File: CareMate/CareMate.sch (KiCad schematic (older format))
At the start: 19 parts, among them J1 Barrel_Jack_MountingPin, J2 Conn_01x16, J3 Conn_01x03, J4 Conn_01x03, J5 Conn_01x06, J6 Conn_01x03, J7 Conn_01x03, J8 Conn_01x02, J9 Conn_01x16, U1 L7805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

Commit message: began running traces
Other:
- note removed: "*Pull up resistor on SD Card Reader\n**Additional Microphone Connect to elechouse and ESP\n***Limit Switch\n****5V Regulator"
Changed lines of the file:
@@
 Wire Wire Line
 	10350 1700 10250 1700
-Text Notes 900  3500 0    50   ~ 0
-*Pull up resistor on SD Card Reader\n**Additional Microphone Connect to elechouse and ESP\n***Limit Switch\n****5V Regulator
 $Comp
 L Regulator_Linear:L7805 U1

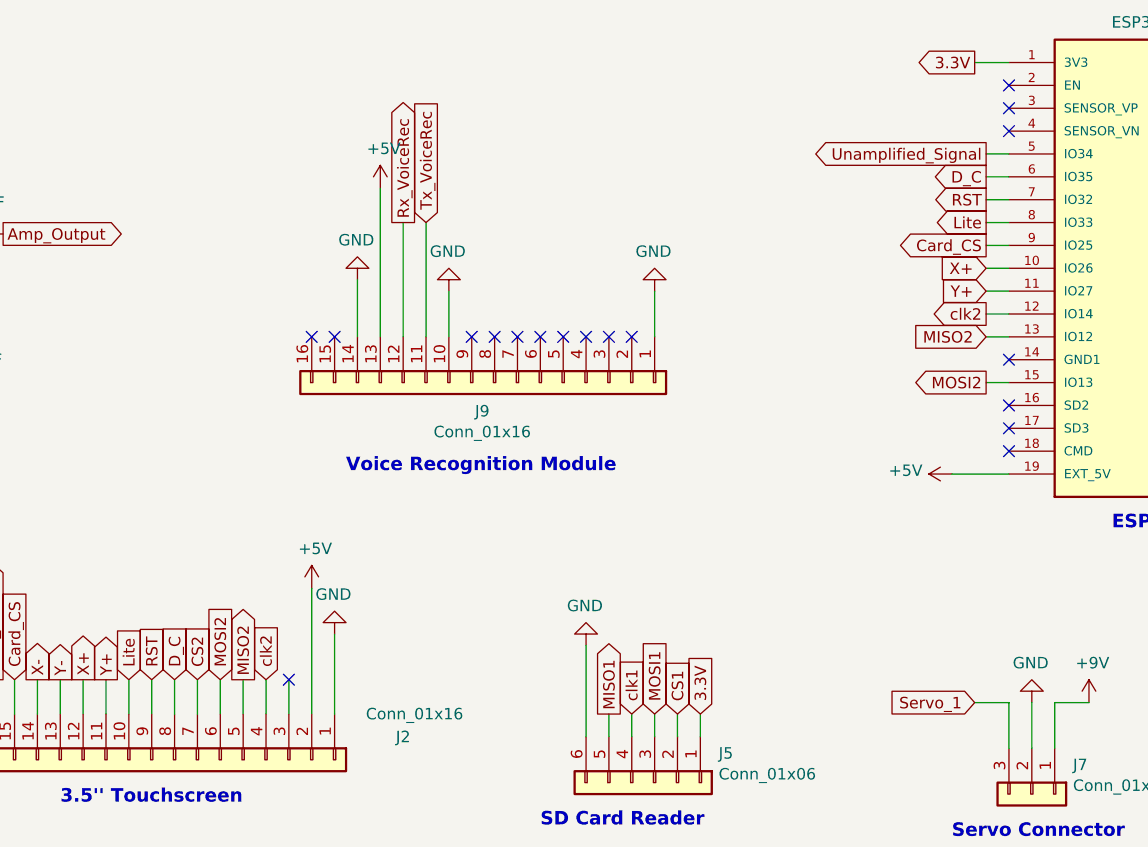
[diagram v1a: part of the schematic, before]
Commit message: Finished routing traces
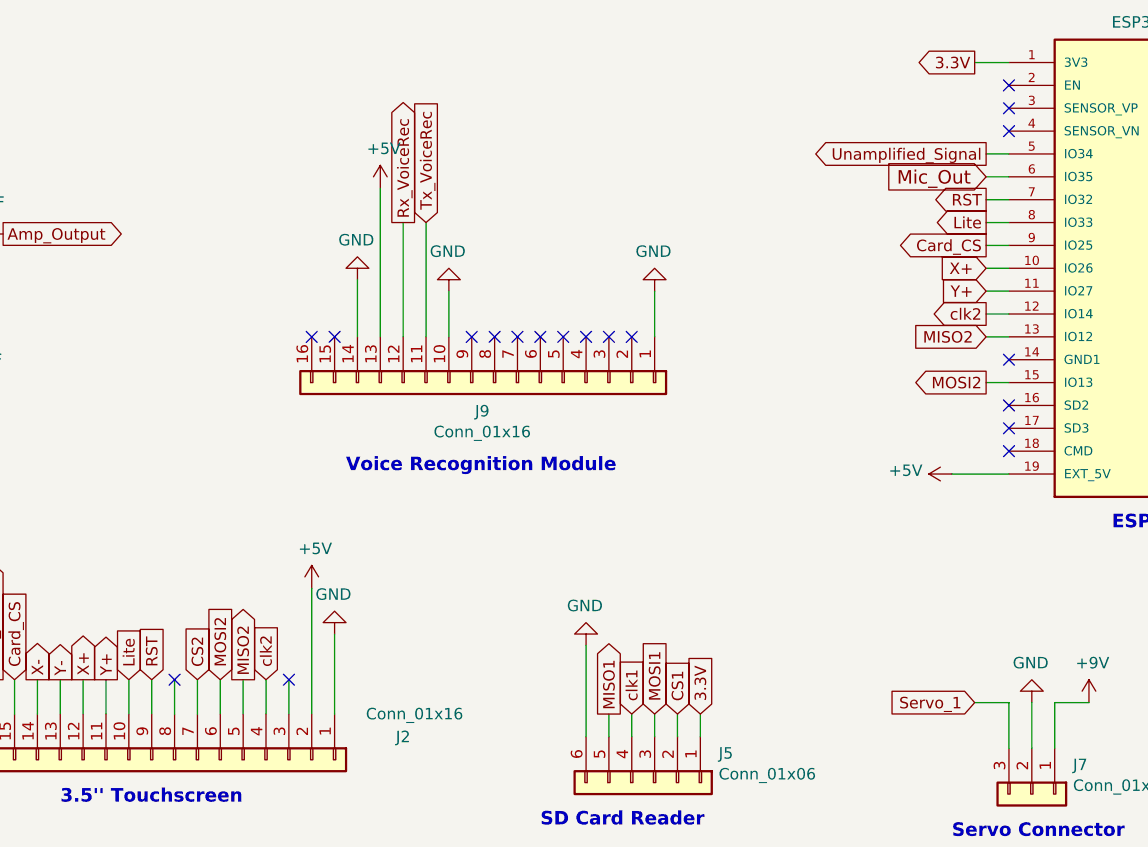
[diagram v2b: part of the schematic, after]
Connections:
- net Mic_Out: now also U4.6 (IO35)
- net D_C: no longer names the net of J2.8 (Pin_8)
- net D_C: no longer U4.6 (IO35)
- no-connect marks 27 -> 28
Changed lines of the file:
@@
 Text GLabel 4900 3900 1    50   Input ~ 0
 RST
-Text GLabel 5000 3900 1    50   Input ~ 0
-D_C
 Text GLabel 4800 3900 1    50   Input ~ 0
 Lite
@@
 Wire Wire Line
 	8650 2300 8550 2300
-Text GLabel 8550 1700 0    50   Output ~ 0
-D_C
 Wire Wire Line
 	8550 1700 8650 1700
@@
 NoConn ~ 6900 2400
 NoConn ~ 7000 2400
+Text GLabel 8550 1700 0    59   Input ~ 0
+Mic_Out
+NoConn ~ 5000 3900
 $EndSCHEMATC

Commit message: PCB second revision
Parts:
- removed J9: Conn_01x16, Additional Libraries:16PinConnector, symbol Connector_Generic:Conn_01x16
- added Conn1, Conn2: Molex_SL_02, Additional Libraries:Easy_2Pin, symbol MRDT_Connectors:Molex_SL_02
- J3, J4, J6, J7: footprint Additional Libraries:3PinConnector_Official -> Additional Libraries:Easy_3Pin
- J8: footprint Additional Libraries:JST_B2B-PH-K-S(LF)(SN) -> Additional Libraries:Easy_2Pin
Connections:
- net GND: now also Conn1.2, Conn2.2
- net Rx_VoiceRec renamed Button_2
- net Button_2: now also Conn1.1
- net Tx_VoiceRec renamed Button_1
- net Button_1: now also Conn2.1
- no-connect marks 28 -> 18
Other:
- note added: "Buttons"
- note removed: "Voice Recognition Module"
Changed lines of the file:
@@
 Unamplified_Signal
 NoConn ~ 3000 1650
-Text GLabel 10350 1500 2    50   Output ~ 0
-Tx_VoiceRec
-Text GLabel 10350 1600 2    50   Input ~ 0
-Rx_VoiceRec
+Text GLabel 10350 1500 2    50   Input ~ 0
+Button_1
 Wire Wire Line
 	10350 1500 10250 1500
@@
 F 0 "J7" V 8622 4580 50  0000 L CNN
 F 1 "Conn_01x03" V 8713 4580 50  0000 L CNN
-F 2 "Additional Libraries:3PinConnector_Official" H 8750 4400 50  0001 C CNN
+F 2 "Additional Libraries:Easy_3Pin" H 8750 4400 50  0001 C CNN
 F 3 "~" H 8750 4400 50  0001 C CNN
 	1    8750 4400
@@
 F 0 "J8" V 10364 4212 50  0000 R CNN
 F 1 "Conn_01x02" V 10273 4212 50  0000 R CNN
-F 2 "Additional Libraries:JST_B2B-PH-K-S(LF)(SN)" H 10400 4400 50  0001 C CNN
+F 2 "Additional Libraries:Easy_2Pin" H 10400 4400 50  0001 C CNN
 F 3 "~" H 10400 4400 50  0001 C CNN
 	1    10400 4400
@@
 Text Notes 1800 2600 0    59   ~ 12
 Amplification Circuit
-Text Notes 5750 3000 0    59   ~ 12
-Voice Recognition Module
 Text Notes 9100 3250 0    59   ~ 12
 ESP32 DevBoard
@@
 F 0 "J3" V 4922 5830 50  0000 L CNN
 F 1 "Conn_01x03" V 5013 5830 50  0000 L CNN
-F 2 "Additional Libraries:3PinConnector_Official" H 5050 5650 50  0001 C CNN
+F 2 "Additional Libraries:Easy_3Pin" H 5050 5650 50  0001 C CNN
 F 3 "~" H 5050 5650 50  0001 C CNN
 	1    5050 5650
@@
 F 0 "J4" V 6722 5930 50  0000 L CNN
 F 1 "Conn_01x03" V 6813 5930 50  0000 L CNN
-F 2 "Additional Libraries:3PinConnector_Official" H 6850 5750 50  0001 C CNN
+F 2 "Additional Libraries:Easy_3Pin" H 6850 5750 50  0001 C CNN
 F 3 "~" H 6850 5750 50  0001 C CNN
 	1    6850 5750
@@
 F 0 "J6" V 7572 5930 50  0000 L CNN
 F 1 "Conn_01x03" V 7663 5930 50  0000 L CNN
-F 2 "Additional Libraries:3PinConnector_Official" H 7700 5750 50  0001 C CNN
+F 2 "Additional Libraries:Easy_3Pin" H 7700 5750 50  0001 C CNN
 F 3 "~" H 7700 5750 50  0001 C CNN
 	1    7700 5750
@@
 	3950 2600 3950 2700
 NoConn ~ 2950 4350
-$Comp
-L Connector_Generic:Conn_01x16 J9
-U 1 1 6144FCF8
-P 6400 2600
-F 0 "J9" V 6525 2546 50  0000 C CNN
-F 1 "Conn_01x16" V 6616 2546 50  0000 C CNN
-F 2 "Additional Libraries:16PinConnector" H 6400 2600 50  0001 C CNN
-F 3 "~" H 6400 2600 50  0001 C CNN
-	1    6400 2600
-	0    1    1    0
-$EndComp
-$Comp
-L power:GND #PWR018
-U 1 1 6146437C
-P 7100 2200
-F 0 "#PWR018" H 7100 1950 50  0001 C CNN
-F 1 "GND" H 7105 2027 50  0000 C CNN
-F 2 "" H 7100 2200 50  0001 C CNN
-F 3 "" H 7100 2200 50  0001 C CNN
-	1    7100 2200
-	-1   0    0    1
-$EndComp
-Wire Wire Line
-	7100 2200 7100 2400
-$Comp
-L power:GND #PWR017
-U 1 1 614683C2
-P 6200 2200
-F 0 "#PWR017" H 6200 1950 50  0001 C CNN
-F 1 "GND" H 6205 2027 50  0000 C CNN
-F 2 "" H 6200 2200 50  0001 C CNN
-F 3 "" H 6200 2200 50  0001 C CNN
-	1    6200 2200
-	-1   0    0    1
-$EndComp
-Wire Wire Line
-	6200 2400 6200 2200
-Text GLabel 6100 1900 1    50   Input ~ 0
-Tx_VoiceRec
-Wire Wire Line
-	6100 1900 6100 2400
-Text GLabel 6000 1900 1    50   Output ~ 0
-Rx_VoiceRec
-Wire Wire Line
-	6000 1900 6000 2400
-$Comp
-L power:+5V #PWR013
-U 1 1 61473728
-P 5900 1750
-F 0 "#PWR013" H 5900 1600 50  0001 C CNN
-F 1 "+5V" H 5915 1923 50  0000 C CNN
-F 2 "" H 5900 1750 50  0001 C CNN
-F 3 "" H 5900 1750 50  0001 C CNN
-	1    5900 1750
-	1    0    0    -1
-$EndComp
-Wire Wire Line
-	5900 1750 5900 2400
-$Comp
-L power:GND #PWR011
-U 1 1 614773AF
-P 5800 2150
-F 0 "#PWR011" H 5800 1900 50  0001 C CNN
-F 1 "GND" H 5805 1977 50  0000 C CNN
-F 2 "" H 5800 2150 50  0001 C CNN
-F 3 "" H 5800 2150 50  0001 C CNN
-	1    5800 2150
-	-1   0    0    1
-$EndComp
-Wire Wire Line
-	5800 2150 5800 2400
-NoConn ~ 5600 2400
-NoConn ~ 5700 2400
-NoConn ~ 6300 2400
-NoConn ~ 6400 2400
-NoConn ~ 6500 2400
-NoConn ~ 6600 2400
-NoConn ~ 6700 2400
-NoConn ~ 6800 2400
-NoConn ~ 6900 2400
-NoConn ~ 7000 2400
+Text GLabel 6550 1900 1    50   Output ~ 0
+Button_1
+Text GLabel 5400 1900 1    50   Output ~ 0
+Button_2
 Text GLabel 8550 1700 0    59   Input ~ 0
 Mic_Out
 NoConn ~ 5000 3900
+Text Notes 5700 2700 0    59   ~ 12
+ Buttons
+$Comp
+L MRDT_Connectors:Molex_SL_02 Conn2
+U 1 1 617F418F
+P 6400 2300
+F 0 "Conn2" V 6289 2538 60  0000 L CNN
+F 1 "Molex_SL_02" V 6395 2538 60  0000 L CNN
+F 2 "Additional Libraries:Easy_2Pin" H 6400 2200 60  0001 C CNN
+F 3 "" H 6400 2200 60  0001 C CNN
+	1    6400 2300
+	0    1    1    0
+$EndComp
+$Comp
+L MRDT_Connectors:Molex_SL_02 Conn1
+U 1 1 617F5383
+P 5250 2300
+F 0 "Conn1" V 5139 2538 60  0000 L CNN
+F 1 "Molex_SL_02" V 5245 2538 60  0000 L CNN
+F 2 "Additional Libraries:Easy_2Pin" H 5250 2200 60  0001 C CNN
+F 3 "" H 5250 2200 60  0001 C CNN
+	1    5250 2300
+	0    1    1    0
+$EndComp
+Wire Wire Line
+	6550 1900 6550 2100
+Wire Wire Line
+	5400 1900 5400 2100
+Text GLabel 10350 1600 2    50   Input ~ 0
+Button_2
+$Comp
+L power:GND #PWR0101
+U 1 1 617FC351
+P 6350 2050
+F 0 "#PWR0101" H 6350 1800 50  0001 C CNN
+F 1 "GND" H 6355 1877 50  0000 C CNN
+F 2 "" H 6350 2050 50  0001 C CNN
+F 3 "" H 6350 2050 50  0001 C CNN
+	1    6350 2050
+	-1   0    0    1
+$EndComp
+Wire Wire Line
+	6450 2100 6350 2100
+Wire Wire Line
+	6350 2100 6350 2050
+$Comp
+L power:GND #PWR0102
+U 1 1 61800077
+P 5200 2050
+F 0 "#PWR0102" H 5200 1800 50  0001 C CNN
+F 1 "GND" H 5205 1877 50  0000 C CNN
+F 2 "" H 5200 2050 50  0001 C CNN
+F 3 "" H 5200 2050 50  0001 C CNN
+	1    5200 2050
+	-1   0    0    1
+$EndComp
+Wire Wire Line
+	5200 2050 5300 2050
+Wire Wire Line
+	5300 2050 5300 2100
 $EndSCHEMATC

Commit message: fixed esp gnd
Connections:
- net GND: now also U4.14 (GND1), U4.20 (GND3), U4.26 (GND2)
- no-connect marks 18 -> 16
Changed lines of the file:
@@
 	8550 1600 8650 1600
-Wire Wire Line
-	8650 2400 8550 2400
 Wire Wire Line
 	8650 2600 8550 2600
@@
 Text GLabel 10350 1700 2    50   Input ~ 0
 LS_2
-NoConn ~ 10250 1800
 NoConn ~ 10250 2200
 NoConn ~ 10250 2800
 NoConn ~ 10250 2900
 NoConn ~ 10250 3000
-NoConn ~ 8650 2500
 NoConn ~ 8650 2700
 NoConn ~ 8650 2800
@@
 Wire Wire Line
 	5300 2050 5300 2100
+Wire Wire Line
+	10250 1200 10850 1200
+$Comp
+L power:GND #PWR?
+U 1 1 61832251
+P 10850 1200
+F 0 "#PWR?" H 10850 950 50  0001 C CNN
+F 1 "GND" H 10855 1027 50  0000 C CNN
+F 2 "" H 10850 1200 50  0001 C CNN
+F 3 "" H 10850 1200 50  0001 C CNN
+	1    10850 1200
+	0    -1   -1   0
+$EndComp
+Wire Wire Line
+	8650 2400 8550 2400
+Wire Wire Line
+	10250 1800 10900 1800
+Wire Wire Line
+	8650 2500 7900 2500
+$Comp
+L power:GND #PWR?
+U 1 1 61838FA1
+P 7900 2500
+F 0 "#PWR?" H 7900 2250 50  0001 C CNN
+F 1 "GND" H 7905 2327 50  0000 C CNN
+F 2 "" H 7900 2500 50  0001 C CNN
+F 3 "" H 7900 2500 50  0001 C CNN
+	1    7900 2500
+	0    1    1    0
+$EndComp
+$Comp
+L power:GND #PWR?
+U 1 1 61839CBB
+P 10900 1800
+F 0 "#PWR?" H 10900 1550 50  0001 C CNN
+F 1 "GND" H 10905 1627 50  0000 C CNN
+F 2 "" H 10900 1800 50  0001 C CNN
+F 3 "" H 10900 1800 50  0001 C CNN
+	1    10900 1800
+	0    -1   -1   0
+$EndComp
 $EndSCHEMATC

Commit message: fixed schematic
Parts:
- removed J6: Conn_01x03, Additional Libraries:Easy_3Pin, symbol Connector_Generic:Conn_01x03
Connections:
- net LS_2 is gone; now on net D_C: U4.25 (IO21)
- net +5V: now also J7.1 (Pin_1)
- net +9V: no longer J7.1 (Pin_1)
- net Button_1: now also U4.5 (IO34); no longer U4.23 (TXD0)
- net Button_2: now also U4.6 (IO35); no longer U4.24 (RXD0)
- net CS1: now also U4.35 (IO15); no longer U4.29 (IO5)
- net CS2: now also U4.30 (IO17); no longer U4.35 (IO15)
- net Card_CS: now also U4.29 (IO5); no longer U4.9 (IO25)
- net GND: no longer U4.14 (GND1)
- net Lite: now also U4.34 (IO2); no longer U4.8 (IO33)
- net MISO1: now also U4.13 (IO12); no longer U4.27 (IO19)
- net MISO2: now also U4.27 (IO19); no longer U4.13 (IO12)
- net MOSI1: now also U4.15 (IO13); no longer U4.21 (IO23)
- net MOSI2: now also U4.21 (IO23); no longer U4.15 (IO13)
- net Mic_Out: now also U4.11 (IO27); no longer U4.6 (IO35)
- net Servo_1: now also U4.10 (IO26); no longer U4.34 (IO2)
- net Unamplified_Signal: now also U4.9 (IO25); no longer U4.5 (IO34)
- net X+: now also U4.32 (IO4); no longer U4.10 (IO26)
- net X-: now also U4.7 (IO32); no longer U4.33 (IO0)
- net Y+: now also U4.8 (IO33); no longer U4.11 (IO27)
- net Y-: now also U4.33 (IO0); no longer U4.32 (IO4)
- net clk1: now also U4.12 (IO14); no longer U4.28 (IO18)
- net clk2: now also U4.28 (IO18); no longer U4.12 (IO14)
- net D_C: now reaches J2.8 (Pin_8)
- net RST: no longer names the net of J2.9 (Pin_9)
- net RST: no longer U4.7 (IO32)
- no-connect marks 16 -> 17
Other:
- note added: "Limit Switch"
- note removed: "Limit Switches"
- note removed: "SCK1"
- note removed: "SS1"
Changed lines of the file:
@@
 Unamplified_Signal
 NoConn ~ 3000 1650
-Text GLabel 10350 1500 2    50   Input ~ 0
+Text GLabel 8550 1600 0    50   Input ~ 0
 Button_1
-Wire Wire Line
-	10350 1500 10250 1500
-Wire Wire Line
-	10250 1600 10350 1600
 $Comp
 L Connector:Barrel_Jack_MountingPin J1
@@
 $EndComp
 $Comp
-L power:+9V #PWR022
-U 1 1 60967D50
-P 9000 4000
-F 0 "#PWR022" H 9000 3850 50  0001 C CNN
-F 1 "+9V" H 9015 4173 50  0000 C CNN
-F 2 "" H 9000 4000 50  0001 C CNN
-F 3 "" H 9000 4000 50  0001 C CNN
-	1    9000 4000
-	1    0    0    -1
-$EndComp
-$Comp
 L power:GND #PWR021
 U 1 1 60968C57
@@
 Text GLabel 8500 4000 0    50   Input ~ 0
 Servo_1
-Text GLabel 10400 2600 2    50   Output ~ 0
+Text GLabel 8550 2100 0    50   Output ~ 0
 Servo_1
 Wire Wire Line
 	10250 2000 10350 2000
-Text GLabel 10350 2000 2    50   Output ~ 0
+Text GLabel 8550 2300 0    50   Output ~ 0
 clk1
 Wire Wire Line
 	10250 1900 10350 1900
-Text GLabel 10350 1900 2    50   Input ~ 0
-MISO1
-Text Notes 10550 2050 0    50   ~ 0
-SCK1
-Text Notes 10550 2150 0    50   ~ 0
-SS1
 Wire Wire Line
 	10250 1300 10350 1300
-Text GLabel 10350 1300 2    50   Output ~ 0
+Text GLabel 8550 2600 0    50   Output ~ 0
 MOSI1
-Text GLabel 10350 2100 2    50   Output ~ 0
+Text GLabel 10400 2700 2    50   Output ~ 0
 CS1
 Wire Wire Line
@@
 Wire Wire Line
 	1950 1850 2700 1850
-Text GLabel 8550 1600 0    50   Output ~ 0
+Text GLabel 8550 2000 0    50   Output ~ 0
 Unamplified_Signal
 Text Notes 2650 4550 0    59   ~ 12
@@
 	5000 4050 5000 3900
 Wire Wire Line
-	4900 4050 4900 3900
-Wire Wire Line
 	4800 4050 4800 3900
 Wire Wire Line
@@
 Text GLabel 5100 3900 1    50   Input ~ 0
 CS2
-Text GLabel 4900 3900 1    50   Input ~ 0
-RST
 Text GLabel 4800 3900 1    50   Input ~ 0
 Lite
@@
 Text Notes 4500 4450 0    59   ~ 12
 3.5'' Touchscreen
-Text GLabel 8550 2400 0    50   Input ~ 0
+Text GLabel 10350 1900 2    50   Input ~ 0
 MISO2
-Text GLabel 8550 2600 0    50   Output ~ 0
+Text GLabel 10350 1300 2    50   Output ~ 0
 MOSI2
-Text GLabel 10400 2700 2    50   Output ~ 0
+Text GLabel 10350 2200 2    50   Output ~ 0
 CS2
 Wire Wire Line
 	8550 1600 8650 1600
-Wire Wire Line
-	8650 2600 8550 2600
-Text GLabel 8550 2300 0    50   Output ~ 0
+Text GLabel 10350 2000 2    50   Output ~ 0
 clk2
 Wire Wire Line
@@
 Wire Wire Line
 	8550 1700 8650 1700
-Text GLabel 8550 1800 0    50   Output ~ 0
-RST
 Wire Wire Line
 	8550 1800 8650 1800
-Text GLabel 8550 1900 0    50   Output ~ 0
+Text GLabel 10350 2600 2    50   Output ~ 0
 Lite
 Wire Wire Line
 	8550 1900 8650 1900
 Wire Wire Line
-	10250 2600 10400 2600
-Wire Wire Line
 	10250 2400 10350 2400
 Wire Wire Line
 	10250 2500 10350 2500
-Text GLabel 8550 2200 0    50   Input ~ 0
+Text GLabel 8550 1900 0    50   Input ~ 0
 Y+
-Text GLabel 8550 2100 0    50   Input ~ 0
+Text GLabel 10350 2400 2    50   Input ~ 0
 X+
-Text GLabel 10350 2400 2    50   Input ~ 0
+Text GLabel 10350 2500 2    50   Input ~ 0
 Y-
-Text GLabel 10350 2500 2    50   Input ~ 0
+Text GLabel 8550 1800 0    50   Input ~ 0
 X-
 Wire Wire Line
@@
 Wire Wire Line
 	8550 2200 8650 2200
-Text GLabel 8550 2000 0    50   Output ~ 0
+Text GLabel 10350 2100 2    50   Output ~ 0
 Card_CS
 Wire Wire Line
@@
 	0    1    1    0
 $EndComp
-$Comp
-L Connector_Generic:Conn_01x03 J6
-U 1 1 61401242
-P 7700 5750
-F 0 "J6" V 7572 5930 50  0000 L CNN
-F 1 "Conn_01x03" V 7663 5930 50  0000 L CNN
-F 2 "Additional Libraries:Easy_3Pin" H 7700 5750 50  0001 C CNN
-F 3 "~" H 7700 5750 50  0001 C CNN
-	1    7700 5750
-	0    1    1    0
-$EndComp
 Text GLabel 6950 5450 1    50   Output ~ 0
 LS_1
 Wire Wire Line
 	6950 5450 6950 5550
-Text GLabel 7800 5450 1    50   Output ~ 0
-LS_2
-Wire Wire Line
-	7800 5450 7800 5550
 Wire Wire Line
 	6750 5550 6750 5450
-Wire Wire Line
-	7600 5550 7600 5450
 Text GLabel 6750 5450 1    50   Input ~ 0
 3.3V
-Text GLabel 7600 5450 1    50   Input ~ 0
-3.3V
 NoConn ~ 6850 5550
-NoConn ~ 7700 5550
 Text GLabel 10350 1400 2    50   Input ~ 0
 LS_1
-Text GLabel 10350 1700 2    50   Input ~ 0
-LS_2
-NoConn ~ 10250 2200
 NoConn ~ 10250 2800
 NoConn ~ 10250 2900
@@
 NoConn ~ 8650 1400
 NoConn ~ 8650 1300
-Text Notes 6950 5950 0    59   ~ 12
-Limit Switches
-Wire Wire Line
-	8400 3000 8650 3000
-$Comp
-L power:+5V #PWR020
-U 1 1 6144058A
-P 8400 3000
-F 0 "#PWR020" H 8400 2850 50  0001 C CNN
-F 1 "+5V" V 8415 3128 50  0000 L CNN
-F 2 "" H 8400 3000 50  0001 C CNN
-F 3 "" H 8400 3000 50  0001 C CNN
-	1    8400 3000
-	0    -1   -1   0
-$EndComp
+Text Notes 6600 5950 0    59   ~ 12
+Limit Switch
 $Comp
 L Device:C_Small C4
@@
 Text GLabel 5400 1900 1    50   Output ~ 0
 Button_2
-Text GLabel 8550 1700 0    59   Input ~ 0
+Text GLabel 8550 2200 0    59   Input ~ 0
 Mic_Out
-NoConn ~ 5000 3900
 Text Notes 5700 2700 0    59   ~ 12
  Buttons
@@
 Wire Wire Line
 	5400 1900 5400 2100
-Text GLabel 10350 1600 2    50   Input ~ 0
+Text GLabel 8550 1700 0    50   Input ~ 0
 Button_2
 $Comp
@@
 Wire Wire Line
 	10250 1800 10900 1800
-Wire Wire Line
-	8650 2500 7900 2500
-$Comp
-L power:GND #PWR?
-U 1 1 61838FA1
-P 7900 2500
-F 0 "#PWR?" H 7900 2250 50  0001 C CNN
-F 1 "GND" H 7905 2327 50  0000 C CNN
-F 2 "" H 7900 2500 50  0001 C CNN
-F 3 "" H 7900 2500 50  0001 C CNN
-	1    7900 2500
-	0    1    1    0
-$EndComp
 $Comp
 L power:GND #PWR?
@@
 	0    -1   -1   0
 $EndComp
+NoConn ~ 8650 2500
+$Comp
+L power:+5V #PWR?
+U 1 1 61854C7E
+P 9000 4000
+F 0 "#PWR?" H 9000 3850 50  0001 C CNN
+F 1 "+5V" H 9015 4173 50  0000 C CNN
+F 2 "" H 9000 4000 50  0001 C CNN
+F 3 "" H 9000 4000 50  0001 C CNN
+	1    9000 4000
+	1    0    0    -1
+$EndComp
+Wire Wire Line
+	10250 2200 10350 2200
+Text GLabel 5000 3900 1    50   Input ~ 0
+D_C
+Text GLabel 10350 1700 2    50   Output ~ 0
+D_C
+Wire Wire Line
+	8650 2600 8550 2600
+Text GLabel 8550 2400 0    50   Input ~ 0
+MISO1
+Wire Wire Line
+	4900 4050 4900 3900
+NoConn ~ 4900 3900
+Wire Wire Line
+	8650 3000 8050 3000
+Wire Wire Line
+	8050 3000 8050 2900
+$Comp
+L power:+5V #PWR?
+U 1 1 6186BFA8
+P 8050 2900
+F 0 "#PWR?" H 8050 2750 50  0001 C CNN
+F 1 "+5V" H 8065 3073 50  0000 C CNN
+F 2 "" H 8050 2900 50  0001 C CNN
+F 3 "" H 8050 2900 50  0001 C CNN
+	1    8050 2900
+	1    0    0    -1
+$EndComp
+Wire Wire Line
+	10250 2600 10350 2600
+NoConn ~ 10250 1500
+NoConn ~ 10250 1600
 $EndSCHEMATC

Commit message: generated gerbs and step
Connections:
- net RST: now reaches J2.9 (Pin_9)
- net RST: now also U4.31 (IO16)
- net Card_Detect: no longer names the net of J2.16 (Pin_16)
- net Card_Detect: no longer U4.31 (IO16)
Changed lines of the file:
@@
 Text GLabel 4400 3900 1    50   Output ~ 0
 X-
-Text GLabel 4200 3900 1    50   Output ~ 0
-Card_Detect
 Text GLabel 4300 3900 1    50   Input ~ 0
 Card_CS
@@
 Wire Wire Line
 	8550 2000 8650 2000
-Text GLabel 10350 2300 2    50   Input ~ 0
-Card_Detect
 Wire Wire Line
 	10350 2300 10250 2300
@@
 	10250 1200 10850 1200
 $Comp
-L power:GND #PWR?
+L power:GND #PWR0103
 U 1 1 61832251
 P 10850 1200
-F 0 "#PWR?" H 10850 950 50  0001 C CNN
+F 0 "#PWR0103" H 10850 950 50  0001 C CNN
 F 1 "GND" H 10855 1027 50  0000 C CNN
 F 2 "" H 10850 1200 50  0001 C CNN
@@
 	10250 1800 10900 1800
 $Comp
-L power:GND #PWR?
+L power:GND #PWR0104
 U 1 1 61839CBB
 P 10900 1800
-F 0 "#PWR?" H 10900 1550 50  0001 C CNN
+F 0 "#PWR0104" H 10900 1550 50  0001 C CNN
 F 1 "GND" H 10905 1627 50  0000 C CNN
 F 2 "" H 10900 1800 50  0001 C CNN
@@
 NoConn ~ 8650 2500
 $Comp
-L power:+5V #PWR?
+L power:+5V #PWR0105
 U 1 1 61854C7E
 P 9000 4000
-F 0 "#PWR?" H 9000 3850 50  0001 C CNN
+F 0 "#PWR0105" H 9000 3850 50  0001 C CNN
 F 1 "+5V" H 9015 4173 50  0000 C CNN
 F 2 "" H 9000 4000 50  0001 C CNN
@@
 Wire Wire Line
 	4900 4050 4900 3900
-NoConn ~ 4900 3900
 Wire Wire Line
 	8650 3000 8050 3000
@@
 	8050 3000 8050 2900
 $Comp
-L power:+5V #PWR?
+L power:+5V #PWR0106
 U 1 1 6186BFA8
 P 8050 2900
-F 0 "#PWR?" H 8050 2750 50  0001 C CNN
+F 0 "#PWR0106" H 8050 2750 50  0001 C CNN
 F 1 "+5V" H 8065 3073 50  0000 C CNN
 F 2 "" H 8050 2900 50  0001 C CNN
@@
 NoConn ~ 10250 1500
 NoConn ~ 10250 1600
+NoConn ~ 4200 3900
+Text GLabel 4900 3900 1    50   Output ~ 0
+RST
+Text GLabel 10350 2300 2    50   Output ~ 0
+RST
 $EndSCHEMATC
